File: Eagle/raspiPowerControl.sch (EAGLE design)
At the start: 15 parts, among them IC1 MCP1702/3 3.3, Q1 DMP3098, T1 BC847

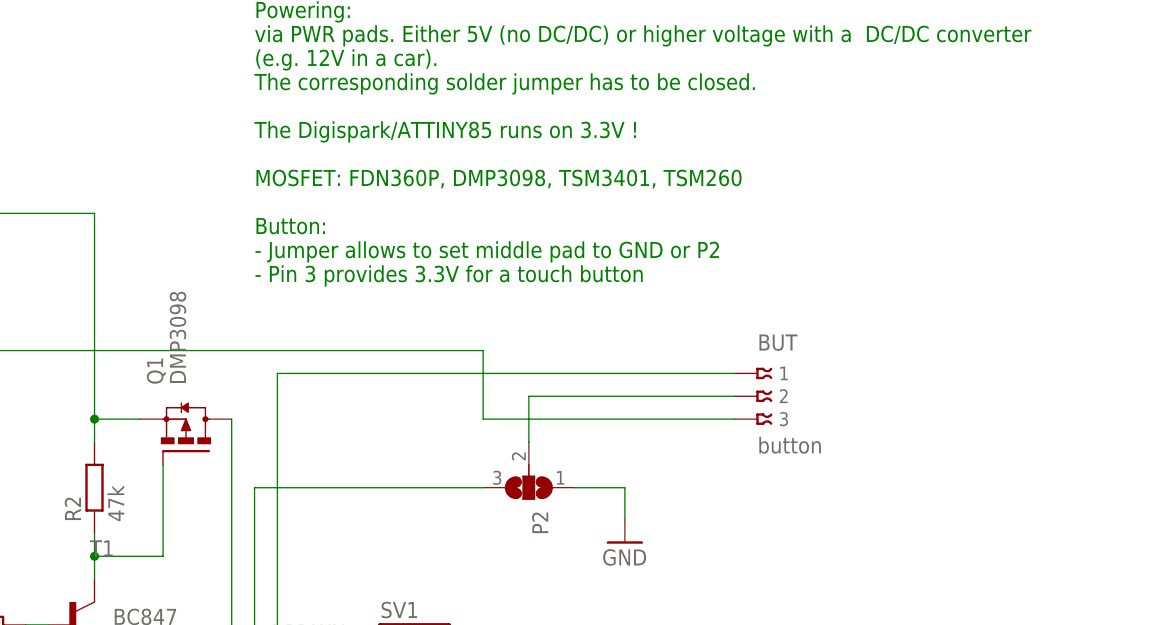
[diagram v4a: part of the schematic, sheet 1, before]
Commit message: Smaller pads for button
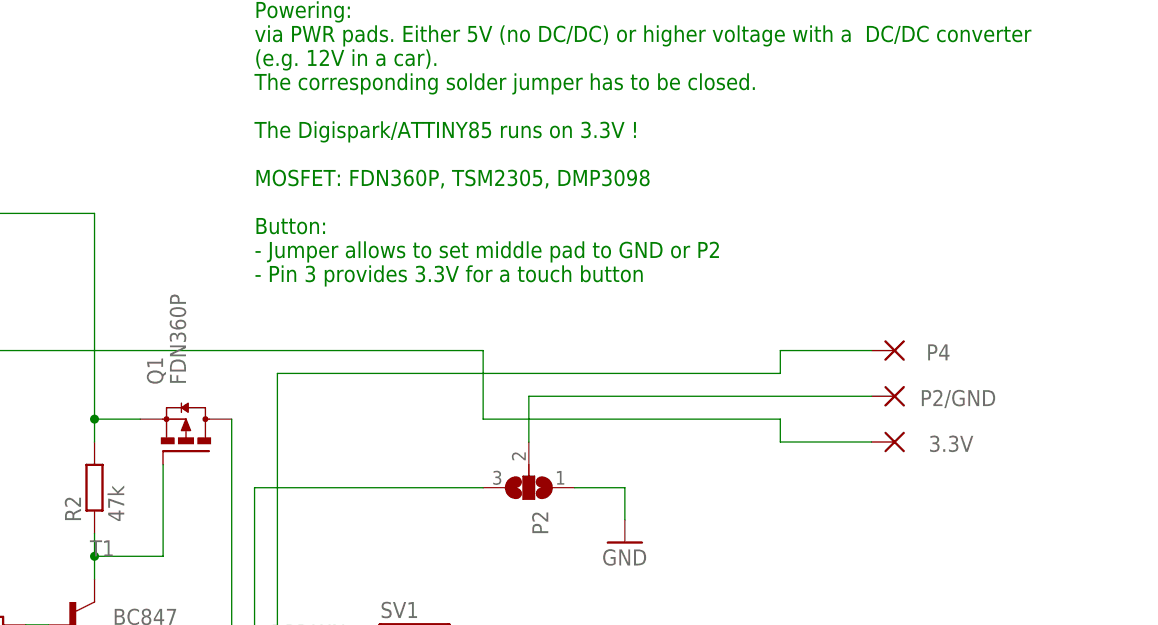
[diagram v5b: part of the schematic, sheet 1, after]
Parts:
- removed BUT: button, con-avx:009176003
- added 3.3V, P2/GND, P4: WIREPADSMD5-1,8, wirepad:WIREPADSMD5-1,8
- Q1: value DMP3098 -> FDN360P
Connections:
- net 3V3: now also 3.3V.P; no longer BUT.3
- net BUT2: now also P2/GND.P; no longer BUT.2
- net BUT4: now also P4.P; no longer BUT.1
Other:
- note added: "Powering: via PWR pads. Either 5V (no DC/DC) or higher voltage with a DC/DC converter (e.g. 12V in a car). The corresponding solder jumper has to be closed. The Digispark/ATTINY85 runs on 3.3V ! MOSFET: FDN360P, TSM2305, DMP3098 Button: - Jumper allows to set middle pad to GND or P2 - Pin 3 provides 3.3V for a touch button"
- note removed: "Powering: via PWR pads. Either 5V (no DC/DC) or higher voltage with a DC/DC converter (e.g. 12V in a car). The corresponding solder jumper has to be closed. The Digispark/ATTINY85 runs on 3.3V ! MOSFET: FDN360P, DMP3098, TSM3401, TSM260 Button: - Jumper allows to set middle pad to GND or P2 - Pin 3 provides 3.3V for a touch button"
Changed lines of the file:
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@@
 <part name="DIGISPARK" library="raspiPowerControl" deviceset="DIGISPARK" device="DIGISPARK-SMD" value="DIGISPARKDIGISPARK-SMD"/>
 <part name="T1" library="transistor-neu-to92" library_urn="urn:adsk.eagle:library:397" deviceset="BC847" device="" package3d_urn="urn:adsk.eagle:package:28738/2"/>
-<part name="Q1" library="transistor-power" library_urn="urn:adsk.eagle:library:400" deviceset="FDN360P" device="" package3d_urn="urn:adsk.eagle:package:29529/2" value="DMP3098"/>
+<part name="Q1" library="transistor-power" library_urn="urn:adsk.eagle:library:400" deviceset="FDN360P" device="" package3d_urn="urn:adsk.eagle:package:29529/2" value="FDN360P"/>
 <part name="GND1" library="supply1" library_urn="urn:adsk.eagle:library:371" deviceset="GND" device=""/>
 <part name="R1" library="rcl" library_urn="urn:adsk.eagle:library:334" deviceset="R-EU_" device="M0805" package3d_urn="urn:adsk.eagle:package:23556/2" value="47k"/>
@@
 <part name="VDD1" library="supply1" library_urn="urn:adsk.eagle:library:371" deviceset="VDD" device="" value="+5V"/>
 <part name="VDD2" library="supply1" library_urn="urn:adsk.eagle:library:371" deviceset="VDD" device="" value="+5V"/>
-<part name="BUT" library="con-avx" library_urn="urn:adsk.eagle:library:129" deviceset="00917?003" device="6" package3d_urn="urn:adsk.eagle:package:6133/1" value="button"/>
 <part name="PWR=5V" library="jumper" library_urn="urn:adsk.eagle:library:252" deviceset="SJ" device="" package3d_urn="urn:adsk.eagle:package:15471/1"/>
 <part name="P2" library="jumper" library_urn="urn:adsk.eagle:library:252" deviceset="SJ2W" device="" package3d_urn="urn:adsk.eagle:package:15474/1"/>
+<part name="3.3V" library="wirepad" library_urn="urn:adsk.eagle:library:412" deviceset="WIREPAD" device="SMD5-1,8" package3d_urn="urn:adsk.eagle:package:30844/1" value=""/>
+<part name="P4" library="wirepad" library_urn="urn:adsk.eagle:library:412" deviceset="WIREPAD" device="SMD5-1,8" package3d_urn="urn:adsk.eagle:package:30844/1" value=""/>
+<part name="P2/GND" library="wirepad" library_urn="urn:adsk.eagle:library:412" deviceset="WIREPAD" device="SMD5-1,8" package3d_urn="urn:adsk.eagle:package:30844/1" value=""/>
 </parts>
 <sheets>
@@
 The corresponding solder jumper has to be closed.
 The Digispark/ATTINY85 runs on 3.3V !
-MOSFET: FDN360P, DMP3098, TSM3401, TSM260
+MOSFET: FDN360P, TSM2305, DMP3098
 Button:
 - Jumper allows to set middle pad to GND or P2
@@
 <attribute name="VALUE" x="20.32" y="101.6" size="1.778" layer="96" rot="R90"/>
 </instance>
-<instance part="BUT" gate="G$1" x="137.16" y="76.2" smashed="yes">
-<attribute name="NAME" x="137.16" y="78.74" size="1.778" layer="95"/>
-<attribute name="VALUE" x="137.16" y="67.31" size="1.778" layer="96"/>
-</instance>
 <instance part="P2" gate="G$1" x="111.76" y="63.5" smashed="yes" rot="R270">
 <attribute name="NAME" x="112.141" y="60.96" size="1.778" layer="95" rot="R270"/>
 <attribute name="VALUE" x="109.855" y="60.96" size="1.778" layer="96" rot="R270"/>
+</instance>
+<instance part="3.3V" gate="G$1" x="152.4" y="68.58" smashed="yes" rot="R180">
+<attribute name="NAME" x="161.163" y="69.2658" size="1.778" layer="95" rot="R180"/>
+<attribute name="VALUE" x="153.543" y="71.882" size="1.778" layer="96" rot="R180"/>
+</instance>
+<instance part="P4" gate="G$1" x="152.4" y="78.74" smashed="yes" rot="R180">
+<attribute name="NAME" x="158.623" y="79.4258" size="1.778" layer="95" rot="R180"/>
+<attribute name="VALUE" x="153.543" y="82.042" size="1.778" layer="96" rot="R180"/>
+</instance>
+<instance part="P2/GND" gate="G$1" x="152.4" y="73.66" smashed="yes" rot="R180">
+<attribute name="NAME" x="163.703" y="74.3458" size="1.778" layer="95" rot="R180"/>
+<attribute name="VALUE" x="153.543" y="76.962" size="1.778" layer="96" rot="R180"/>
 </instance>
 </instances>
@@
 <wire x1="45.72" y1="78.74" x2="45.72" y2="20.32" width="0.1524" layer="91"/>
 <wire x1="45.72" y1="20.32" x2="35.56" y2="20.32" width="0.1524" layer="91"/>
-<wire x1="134.62" y1="71.12" x2="106.68" y2="71.12" width="0.1524" layer="91"/>
+<wire x1="139.7" y1="71.12" x2="106.68" y2="71.12" width="0.1524" layer="91"/>
 <wire x1="106.68" y1="71.12" x2="106.68" y2="78.74" width="0.1524" layer="91"/>
 <wire x1="106.68" y1="78.74" x2="45.72" y2="78.74" width="0.1524" layer="91"/>
 <junction x="45.72" y="78.74"/>
-<pinref part="BUT" gate="G$1" pin="3"/>
+<wire x1="139.7" y1="71.12" x2="139.7" y2="68.58" width="0.1524" layer="91"/>
+<pinref part="3.3V" gate="G$1" pin="P"/>
+<wire x1="139.7" y1="68.58" x2="149.86" y2="68.58" width="0.1524" layer="91"/>
 </segment>
 </net>
@@
 <wire x1="5.08" y1="40.64" x2="83.82" y2="40.64" width="0.1524" layer="91"/>
 <wire x1="83.82" y1="40.64" x2="83.82" y2="76.2" width="0.1524" layer="91"/>
-<wire x1="83.82" y1="76.2" x2="134.62" y2="76.2" width="0.1524" layer="91"/>
-<pinref part="BUT" gate="G$1" pin="1"/>
+<wire x1="83.82" y1="76.2" x2="139.7" y2="76.2" width="0.1524" layer="91"/>
+<wire x1="139.7" y1="76.2" x2="139.7" y2="78.74" width="0.1524" layer="91"/>
+<pinref part="P4" gate="G$1" pin="P"/>
+<wire x1="139.7" y1="78.74" x2="149.86" y2="78.74" width="0.1524" layer="91"/>
 </segment>
 </net>
@@
 <pinref part="P2" gate="G$1" pin="2"/>
 <wire x1="111.76" y1="68.58" x2="111.76" y2="73.66" width="0.1524" layer="91"/>
-<pinref part="BUT" gate="G$1" pin="2"/>
-<wire x1="134.62" y1="73.66" x2="111.76" y2="73.66" width="0.1524" layer="91"/>
-</segment>
-</net>
+<wire x1="149.86" y1="73.66" x2="111.76" y2="73.66" width="0.1524" layer="91"/>
+<pinref part="P2/GND" gate="G$1" pin="P"/>
+</segment>
+</net>

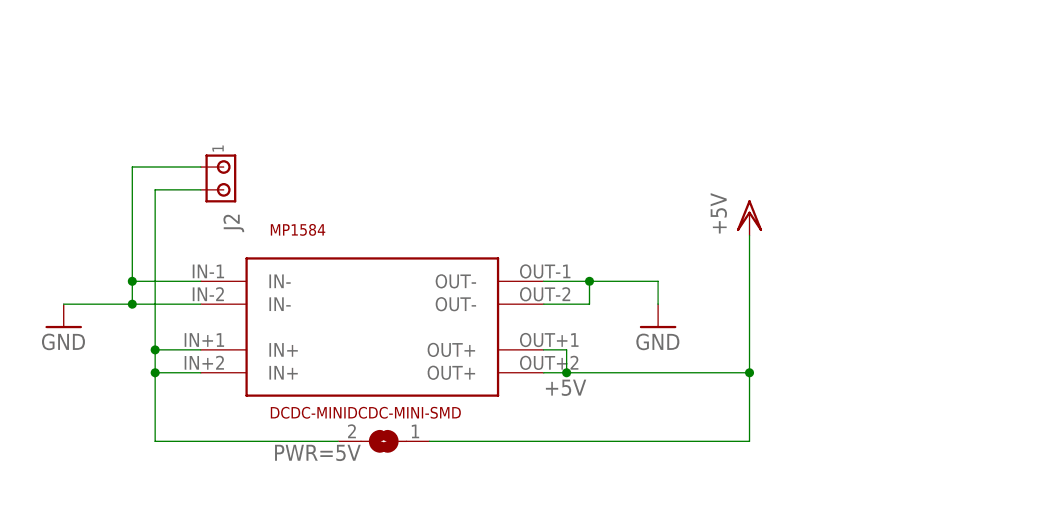
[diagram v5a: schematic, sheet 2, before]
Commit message: Add JLC PCB and assembly files
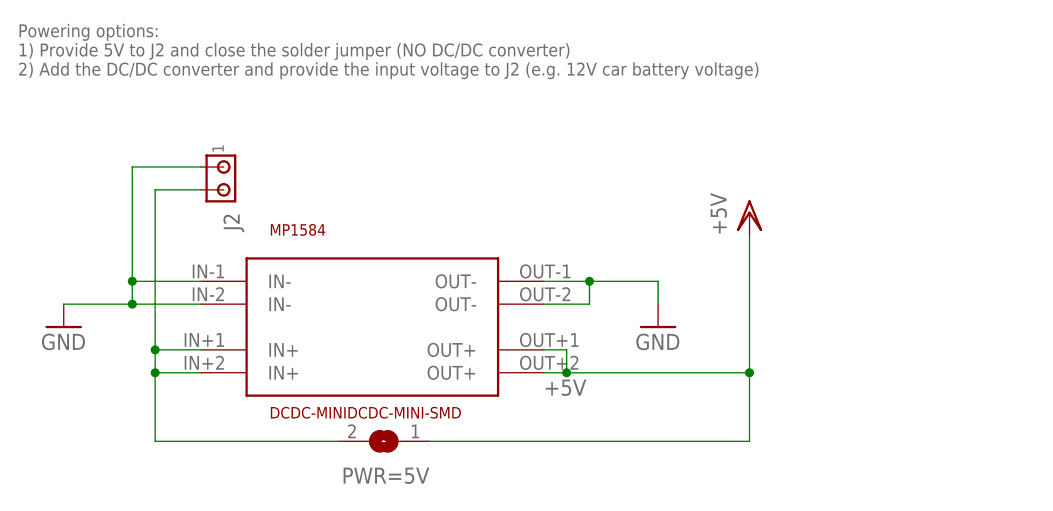
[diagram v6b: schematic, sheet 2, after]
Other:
- note added: "Powering options: 1) Provide 5V to J2 and close the solder jumper (NO DC/DC converter) 2) Add the DC/DC converter and provide the input voltage to J2 (e.g. 12V car battery voltage)"
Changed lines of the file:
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@@
 <description>Addition for 12V car battery powering</description>
 <plain>
+<text x="7.62" y="48.26" size="1.4224" layer="95">Powering options:
+1) Provide 5V to J2 and close the solder jumper (NO DC/DC converter)
+2) Add the DC/DC converter and provide the input voltage to J2 (e.g. 12V car battery voltage)</text>
 </plain>
 <instances>
@@
 </instance>
 <instance part="PWR=5V" gate="1" x="48.26" y="7.62" smashed="yes" rot="R180">
-<attribute name="NAME" x="45.72" y="7.239" size="1.778" layer="95" rot="R180"/>
+<attribute name="NAME" x="53.34" y="4.699" size="1.778" layer="95" rot="R180"/>
 <attribute name="VALUE" x="45.72" y="9.525" size="1.778" layer="96" rot="R180"/>
 </instance>
